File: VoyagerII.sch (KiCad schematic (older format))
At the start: 5 parts, among them U1 ATXMEGA32A4U-AU

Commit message: Voltage tests
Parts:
- added C?: 1u, symbol C_Small
- added D?: D_Schottky_Small, symbol D_Schottky_Small
- added U?: MCP1700T-3002E/TT, TO_SOT_Packages_SMD:SOT-23, symbol MCP1700-3002E_SOT23
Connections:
- net +5V: now also U?.3 (VI)
- net GND: now also C?.2, U?.1 (GND)
- new net: C?.1, D?.2 (A), U?.2 (VO)
- new net +3V3: D?.1 (K)
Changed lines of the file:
@@
+	1    0    0    -1
+$EndComp
+$Comp
+L MCP1700-3002E_SOT23 U?
+U 1 1 5A6246D3
+P 3950 1175
+F 0 "U?" H 3800 1300 50  0000 C CNN
+F 1 "MCP1700T-3002E/TT" H 3575 1400 50  0000 L CNN
+F 2 "TO_SOT_Packages_SMD:SOT-23" H 3950 1400 50  0001 C CNN
+F 3 "" H 3950 1175 50  0001 C CNN
+	1    3950 1175
+	1    0    0    -1
+$EndComp
+$Comp
+L +5V #PWR?
+U 1 1 5A624862
+P 3650 1175
+F 0 "#PWR?" H 3650 1025 50  0001 C CNN
+F 1 "+5V" H 3650 1315 50  0000 C CNN
+F 2 "" H 3650 1175 50  0001 C CNN
+F 3 "" H 3650 1175 50  0001 C CNN
+	1    3650 1175
+	0    -1   -1   0
+$EndComp
+$Comp
+L GND #PWR?
+U 1 1 5A6248B2
+P 3950 1475
+F 0 "#PWR?" H 3950 1225 50  0001 C CNN
+F 1 "GND" H 3950 1325 50  0000 C CNN
+F 2 "" H 3950 1475 50  0001 C CNN
+F 3 "" H 3950 1475 50  0001 C CNN
+	1    3950 1475
+	1    0    0    -1
+$EndComp
+$Comp
+L C_Small C?
+U 1 1 5A6248D2
+P 4325 1275
+F 0 "C?" H 4335 1345 50  0000 L CNN
+F 1 "1u" H 4335 1195 50  0000 L CNN
+F 2 "" H 4325 1275 50  0001 C CNN
+F 3 "" H 4325 1275 50  0001 C CNN
+	1    4325 1275
+	1    0    0    -1
+$EndComp
+Wire Wire Line
+	4250 1175 4525 1175
+$Comp
+L D_Schottky_Small D?
+U 1 1 5A624ACB
+P 4625 1175
+F 0 "D?" H 4575 1255 50  0000 L CNN
+F 1 "D_Schottky_Small" H 4345 1095 50  0000 L CNN
+F 2 "" V 4625 1175 50  0001 C CNN
+F 3 "" V 4625 1175 50  0001 C CNN
+	1    4625 1175
+	-1   0    0    1
+$EndComp
+Connection ~ 4325 1175
+$Comp
+L +3.3V #PWR?
+U 1 1 5A624B50
+P 4900 1175
+F 0 "#PWR?" H 4900 1025 50  0001 C CNN
+F 1 "+3.3V" H 4900 1315 50  0000 C CNN
+F 2 "" H 4900 1175 50  0001 C CNN
+F 3 "" H 4900 1175 50  0001 C CNN
+	1    4900 1175
+	-1   0    0    1
+$EndComp
+Wire Wire Line
+	4900 1175 4725 1175
+$Comp
+L GND #PWR?
+U 1 1 5A624D2D
+P 4325 1375
+F 0 "#PWR?" H 4325 1125 50  0001 C CNN
+F 1 "GND" H 4325 1225 50  0000 C CNN
+F 2 "" H 4325 1375 50  0001 C CNN
+F 3 "" H 4325 1375 50  0001 C CNN
+	1    4325 1375
 	1    0    0    -1
 $EndComp

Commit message: Continue schematic
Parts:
- added R?: 10k, symbol R_Small
- added R? (x2): R_Small, symbol R_Small
- added SW?: SW_PUSH, symbol SW_PUSH
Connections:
- net +3V3: now also R?.1
- net +5V: now also R?.2
- net GND: now also R?.1, SW?.1
- net D-: now reaches U1.26 (PD6/D-/RXD1/MISO)
- net D+: now reaches U1.27 (PD7/D+/TXD1/SCK/CLKOUT/EVOUT)
- net at U1.32 (PE2/OC0C/RXD0): now also R?.1, R?.2
- net at U1.35 (~RESET~/PDI_CLK): now also R?.2, SW?.2
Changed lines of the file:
@@
 LIBS:switches
 LIBS:relays
-LIBS:motors
 LIBS:transistors
 LIBS:conn
@@
 	1    0    0    -1
 $EndComp
+$Comp
+L R_Small R?
+U 1 1 5A62554E
+P 2675 3075
+F 0 "R?" H 2705 3095 50  0000 L CNN
+F 1 "10k" H 2705 3035 50  0000 L CNN
+F 2 "" H 2675 3075 50  0000 C CNN
+F 3 "" H 2675 3075 50  0000 C CNN
+	1    2675 3075
+	1    0    0    -1
+$EndComp
+Wire Wire Line
+	2675 3175 2900 3175
+$Comp
+L +3.3V #PWR?
+U 1 1 5A625634
+P 2675 2975
+F 0 "#PWR?" H 2675 2825 50  0001 C CNN
+F 1 "+3.3V" H 2675 3115 50  0000 C CNN
+F 2 "" H 2675 2975 50  0000 C CNN
+F 3 "" H 2675 2975 50  0000 C CNN
+	1    2675 2975
+	1    0    0    -1
+$EndComp
+$Comp
+L SW_PUSH SW?
+U 1 1 5A62565A
+P 2375 3175
+F 0 "SW?" H 2525 3285 50  0000 C CNN
+F 1 "SW_PUSH" H 2375 3095 50  0000 C CNN
+F 2 "" H 2375 3175 50  0000 C CNN
+F 3 "" H 2375 3175 50  0000 C CNN
+	1    2375 3175
+	1    0    0    -1
+$EndComp
+$Comp
+L GND #PWR?
+U 1 1 5A625723
+P 2075 3175
+F 0 "#PWR?" H 2075 2925 50  0001 C CNN
+F 1 "GND" H 2075 3025 50  0000 C CNN
+F 2 "" H 2075 3175 50  0000 C CNN
+F 3 "" H 2075 3175 50  0000 C CNN
+	1    2075 3175
+	0    1    1    0
+$EndComp
+$Comp
+L R_Small R?
+U 1 1 5A6258EE
+P 2525 4050
+F 0 "R?" H 2555 4070 50  0000 L CNN
+F 1 "R_Small" H 2555 4010 50  0000 L CNN
+F 2 "" H 2525 4050 50  0000 C CNN
+F 3 "" H 2525 4050 50  0000 C CNN
+	1    2525 4050
+	-1   0    0    1
+$EndComp
+$Comp
+L R_Small R?
+U 1 1 5A625956
+P 2525 4400
+F 0 "R?" H 2555 4420 50  0000 L CNN
+F 1 "R_Small" H 2555 4360 50  0000 L CNN
+F 2 "" H 2525 4400 50  0000 C CNN
+F 3 "" H 2525 4400 50  0000 C CNN
+	1    2525 4400
+	-1   0    0    1
+$EndComp
+Wire Wire Line
+	2525 4150 2525 4300
+Wire Wire Line
+	2900 4225 2525 4225
+Connection ~ 2525 4225
+$Comp
+L +5V #PWR?
+U 1 1 5A6259CA
+P 2525 3950
+F 0 "#PWR?" H 2525 3800 50  0001 C CNN
+F 1 "+5V" H 2525 4090 50  0000 C CNN
+F 2 "" H 2525 3950 50  0000 C CNN
+F 3 "" H 2525 3950 50  0000 C CNN
+	1    2525 3950
+	1    0    0    -1
+$EndComp
+$Comp
+L GND #PWR?
+U 1 1 5A6259F6
+P 2525 4500
+F 0 "#PWR?" H 2525 4250 50  0001 C CNN
+F 1 "GND" H 2525 4350 50  0000 C CNN
+F 2 "" H 2525 4500 50  0000 C CNN
+F 3 "" H 2525 4500 50  0000 C CNN
+	1    2525 4500
+	1    0    0    -1
+$EndComp
+Text GLabel 2900 5075 0    60   Input ~ 0
+D-
+Text GLabel 2900 5175 0    60   Input ~ 0
+D+
 $EndSCHEMATC

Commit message: Add libs
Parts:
- added C? (x5): 0.1u, symbol C_Small
- added C?: 4.7u, symbol C_Small
- added P?: TC2030-IDC, symbol TC2030-IDC
- R? (x2): value R_Small -> 100k
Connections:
- net +3V3: now also U1.19 (VCC), U1.31 (VCC), U1.39 (AVCC), U1.9 (VCC), C?.1, C?.1, C?.1, C?.1, C?.1
- net GND: now also U1.18 (GND), U1.30 (GND), U1.38 (GND), U1.8 (GND), C?.1, C?.2, C?.2, C?.2, C?.2, C?.2, C?.2, P?.2 (P2), P?.6 (P6)
- net PDI: now reaches U1.34 (PDI_DATA)
- net PDI: now also P?.1 (P1)
- net PDI_CLK: now reaches R?.2, SW?.2, U1.35 (~RESET~/PDI_CLK)
- net PDI_CLK: now also P?.5 (P5)
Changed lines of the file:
@@
 LIBS:MX_Alps_Hybrids
 LIBS:ws2812b
+LIBS:Tag-Connect
 LIBS:VoyagerII-cache
 EELAYER 25 0
@@
 P 2525 4050
 F 0 "R?" H 2555 4070 50  0000 L CNN
-F 1 "R_Small" H 2555 4010 50  0000 L CNN
+F 1 "100k" H 2555 4010 50  0000 L CNN
 F 2 "" H 2525 4050 50  0000 C CNN
 F 3 "" H 2525 4050 50  0000 C CNN
@@
 P 2525 4400
 F 0 "R?" H 2555 4420 50  0000 L CNN
-F 1 "R_Small" H 2555 4360 50  0000 L CNN
+F 1 "100k" H 2555 4360 50  0000 L CNN
 F 2 "" H 2525 4400 50  0000 C CNN
 F 3 "" H 2525 4400 50  0000 C CNN
@@
 Text GLabel 2900 5175 0    60   Input ~ 0
 D+
+$Comp
+L TC2030-IDC P?
+U 1 1 5A625E7B
+P 1350 2525
+F 0 "P?" H 1300 2325 40  0000 L CNN
+F 1 "TC2030-IDC" H 1350 2725 40  0000 C CNN
+F 2 "" H 1350 2525 60  0000 C CNN
+F 3 "" H 1350 2525 60  0000 C CNN
+	1    1350 2525
+	1    0    0    -1
+$EndComp
+Text GLabel 1100 2425 0    60   Input ~ 0
+PDI
+Text GLabel 1100 2625 0    60   Input ~ 0
+PDI_CLK
+$Comp
+L GND #PWR?
+U 1 1 5A62606A
+P 1600 2625
+F 0 "#PWR?" H 1600 2375 50  0001 C CNN
+F 1 "GND" H 1600 2475 50  0000 C CNN
+F 2 "" H 1600 2625 50  0000 C CNN
+F 3 "" H 1600 2625 50  0000 C CNN
+	1    1600 2625
+	0    -1   -1   0
+$EndComp
+$Comp
+L C_Small C?
+U 1 1 5A626098
+P 1650 2325
+F 0 "C?" H 1660 2395 50  0000 L CNN
+F 1 "0.1u" H 1660 2245 50  0000 L CNN
+F 2 "" H 1650 2325 50  0000 C CNN
+F 3 "" H 1650 2325 50  0000 C CNN
+	1    1650 2325
+	1    0    0    -1
+$EndComp
+Wire Wire Line
+	1600 2425 1850 2425
+$Comp
+L GND #PWR?
+U 1 1 5A626190
+P 1650 2225
+F 0 "#PWR?" H 1650 1975 50  0001 C CNN
+F 1 "GND" H 1650 2075 50  0000 C CNN
+F 2 "" H 1650 2225 50  0000 C CNN
+F 3 "" H 1650 2225 50  0000 C CNN
+	1    1650 2225
+	-1   0    0    1
+$EndComp
+$Comp
+L GND #PWR?
+U 1 1 5A6261C0
+P 1850 2425
+F 0 "#PWR?" H 1850 2175 50  0001 C CNN
+F 1 "GND" H 1850 2275 50  0000 C CNN
+F 2 "" H 1850 2425 50  0000 C CNN
+F 3 "" H 1850 2425 50  0000 C CNN
+	1    1850 2425
+	0    -1   -1   0
+$EndComp
+Connection ~ 1650 2425
+Wire Wire Line
+	2900 3175 2900 3000
+Text GLabel 2900 3000 1    60   Input ~ 0
+PDI_CLK
+Text GLabel 2900 3275 0    60   Input ~ 0
+PDI
+Wire Wire Line
+	3700 2875 3700 2725
+Wire Wire Line
+	3700 2725 4100 2725
+Wire Wire Line
+	3800 2725 3800 2875
+Wire Wire Line
+	3900 2725 3900 2875
+Connection ~ 3800 2725
+Wire Wire Line
+	4100 2725 4100 2875
+Connection ~ 3900 2725
+$Comp
+L +3.3V #PWR?
+U 1 1 5A6265F5
+P 3700 2725
+F 0 "#PWR?" H 3700 2575 50  0001 C CNN
+F 1 "+3.3V" H 3700 2865 50  0000 C CNN
+F 2 "" H 3700 2725 50  0000 C CNN
+F 3 "" H 3700 2725 50  0000 C CNN
+	1    3700 2725
+	1    0    0    -1
+$EndComp
+Wire Wire Line
+	3950 5625 3950 5475
+Wire Wire Line
+	3650 5625 3950 5625
+Wire Wire Line
+	3850 5625 3850 5475
+Wire Wire Line
+	3750 5625 3750 5475
+Connection ~ 3850 5625
+Wire Wire Line
+	3650 5625 3650 5475
+Connection ~ 3750 5625
+$Comp
+L GND #PWR?
+U 1 1 5A626934
+P 3950 5625
+F 0 "#PWR?" H 3950 5375 50  0001 C CNN
+F 1 "GND" H 3950 5475 50  0000 C CNN
+F 2 "" H 3950 5625 50  0000 C CNN
+F 3 "" H 3950 5625 50  0000 C CNN
+	1    3950 5625
+	1    0    0    -1
+$EndComp
+$Comp
+L C_Small C?
+U 1 1 5A626BEB
+P 4225 2175
+F 0 "C?" H 4235 2245 50  0000 L CNN
+F 1 "0.1u" H 4235 2095 50  0000 L CNN
+F 2 "" H 4225 2175 50  0000 C CNN
+F 3 "" H 4225 2175 50  0000 C CNN
+	1    4225 2175
+	1    0    0    -1
+$EndComp
+$Comp
+L C_Small C?
+U 1 1 5A626C99
+P 4625 2175
+F 0 "C?" H 4635 2245 50  0000 L CNN
+F 1 "0.1u" H 4635 2095 50  0000 L CNN
+F 2 "" H 4625 2175 50  0000 C CNN
+F 3 "" H 4625 2175 50  0000 C CNN
+	1    4625 2175
+	1    0    0    -1
+$EndComp
+$Comp
+L C_Small C?
+U 1 1 5A626CEB
+P 4825 2175
+F 0 "C?" H 4835 2245 50  0000 L CNN
+F 1 "0.1u" H 4835 2095 50  0000 L CNN
+F 2 "" H 4825 2175 50  0000 C CNN
+F 3 "" H 4825 2175 50  0000 C CNN
+	1    4825 2175
+	1    0    0    -1
+$EndComp
+$Comp
+L C_Small C?
+U 1 1 5A626D3A
+P 4425 2175
+F 0 "C?" H 4435 2245 50  0000 L CNN
+F 1 "0.1u" H 4435 2095 50  0000 L CNN
+F 2 "" H 4425 2175 50  0000 C CNN
+F 3 "" H 4425 2175 50  0000 C CNN
+	1    4425 2175
+	1    0    0    -1
+$EndComp
+$Comp
+L C_Small C?
+U 1 1 5A626DD8
+P 5050 2175
+F 0 "C?" H 5060 2245 50  0000 L CNN
+F 1 "4.7u" H 5060 2095 50  0000 L CNN
+F 2 "" H 5050 2175 50  0000 C CNN
+F 3 "" H 5050 2175 50  0000 C CNN
+	1    5050 2175
+	1    0    0    -1
+$EndComp
+Wire Wire Line
+	4225 2275 5050 2275
+Connection ~ 4825 2275
+Connection ~ 4625 2275
+Connection ~ 4425 2275
+Wire Wire Line
+	4225 2075 5050 2075
+Connection ~ 4425 2075
+Connection ~ 4625 2075
+Connection ~ 4825 2075
+$Comp
+L +3.3V #PWR?
+U 1 1 5A627061
+P 4225 2075
+F 0 "#PWR?" H 4225 1925 50  0001 C CNN
+F 1 "+3.3V" H 4225 2215 50  0000 C CNN
+F 2 "" H 4225 2075 50  0000 C CNN
+F 3 "" H 4225 2075 50  0000 C CNN
+	1    4225 2075
+	1    0    0    -1
+$EndComp
+$Comp
+L GND #PWR?
+U 1 1 5A62709B
+P 4225 2275
+F 0 "#PWR?" H 4225 2025 50  0001 C CNN
+F 1 "GND" H 4225 2125 50  0000 C CNN
+F 2 "" H 4225 2275 50  0000 C CNN
+F 3 "" H 4225 2275 50  0000 C CNN
+	1    4225 2275
+	1    0    0    -1
+$EndComp
 $EndSCHEMATC

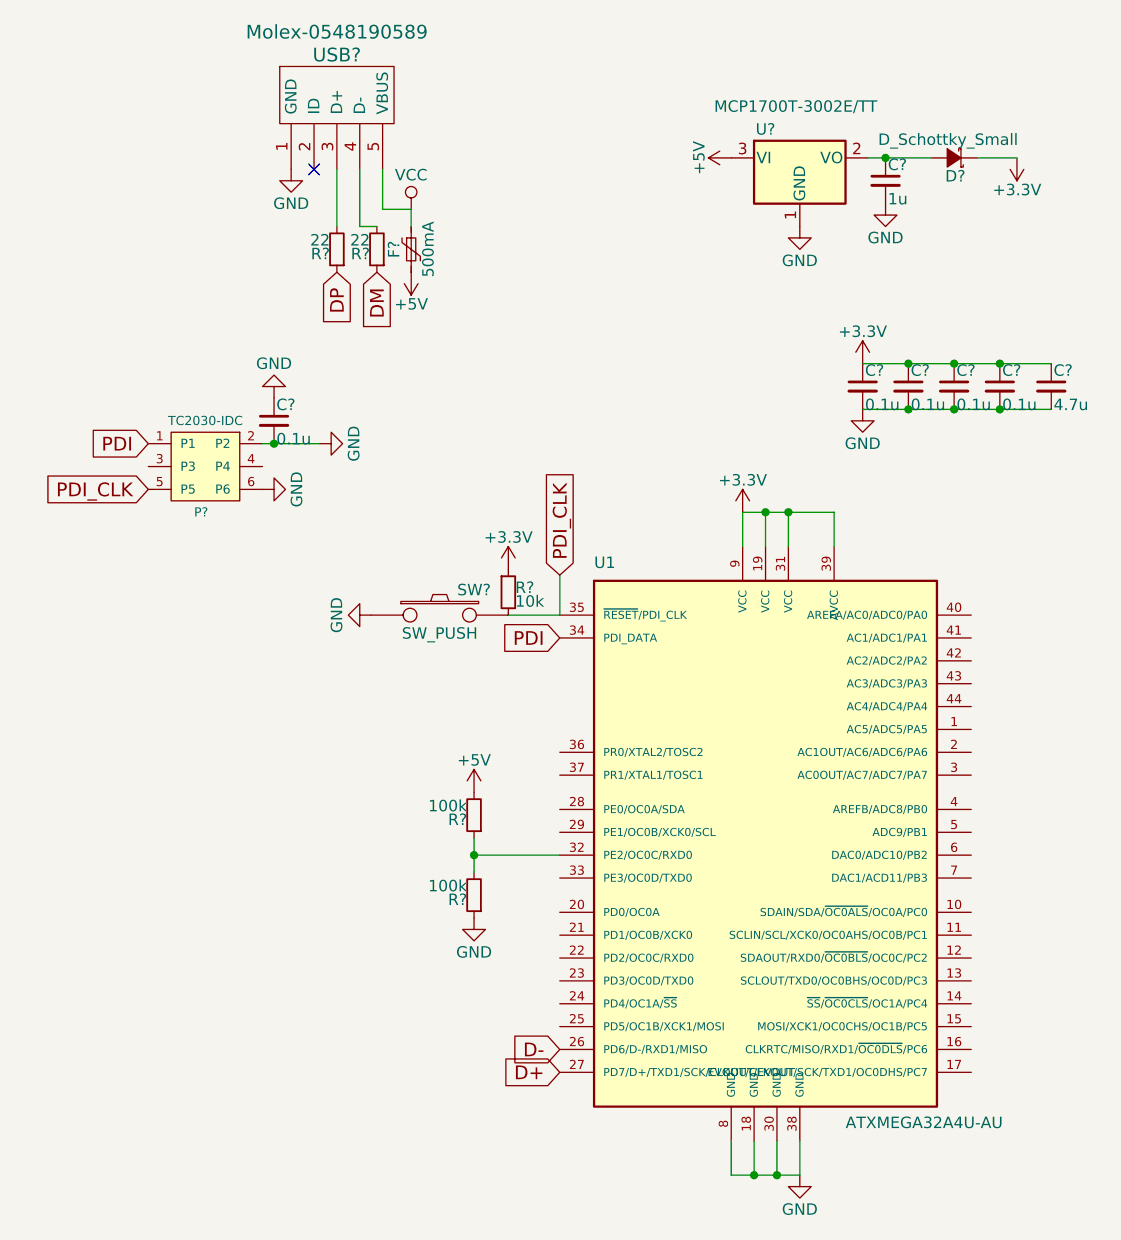
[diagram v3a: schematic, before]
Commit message: Tune up controller to final state
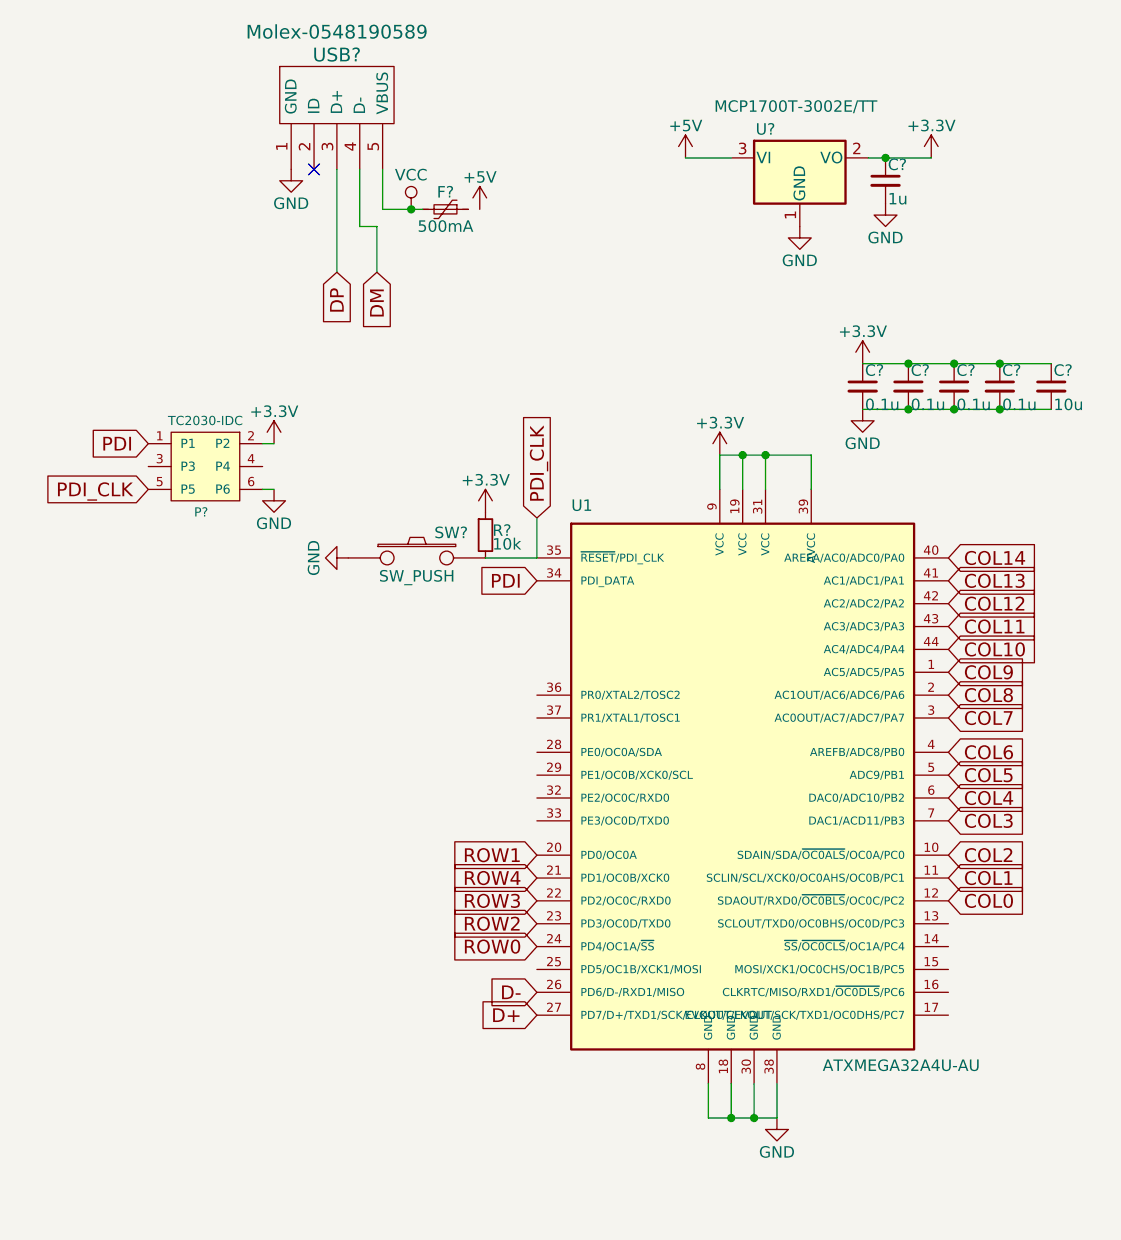
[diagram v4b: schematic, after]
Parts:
- removed C?: 0.1u, symbol C_Small
- removed D?: D_Schottky_Small, symbol D_Schottky_Small
- removed R? (x2): 22, symbol R_Small
- removed R? (x2): 100k, symbol R_Small
- C?: value 4.7u -> 10u
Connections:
- net +3V3: now also C?.1, P?.2 (P2), U?.2 (VO)
- net +5V: no longer F?.2
- net DM: now also USB?.4 (D-)
- net DP: now also USB?.3 (D+)
- net GND: no longer P?.2 (P2)
- net VCC: now also F?.2; no longer F?.1
- net COL9: now reaches U1.1 (AC5/ADC5/PA5)
- net COL2: now reaches U1.10 (SDAIN/SDA/~OC0ALS~/OC0A/PC0)
- net COL1: now reaches U1.11 (SCLIN/SCL/XCK0/OC0AHS/OC0B/PC1)
- net COL0: now reaches U1.12 (SDAOUT/RXD0/~OC0BLS~/OC0C/PC2)
- net COL8: now reaches U1.2 (AC1OUT/AC6/ADC6/PA6)
- net ROW1: now reaches U1.20 (PD0/OC0A)
- net ROW4: now reaches U1.21 (PD1/OC0B/XCK0)
- net ROW3: now reaches U1.22 (PD2/OC0C/RXD0)
- net ROW2: now reaches U1.23 (PD3/OC0D/TXD0)
- net ROW0: now reaches U1.24 (PD4/OC1A/~SS~)
- net COL7: now reaches U1.3 (AC0OUT/AC7/ADC7/PA7)
- net COL6: now reaches U1.4 (AREFB/ADC8/PB0)
- net COL14: now reaches U1.40 (AREFA/AC0/ADC0/PA0)
- net COL13: now reaches U1.41 (AC1/ADC1/PA1)
- net COL12: now reaches U1.42 (AC2/ADC2/PA2)
- net COL11: now reaches U1.43 (AC3/ADC3/PA3)
- net COL10: now reaches U1.44 (AC4/ADC4/PA4)
- net COL5: now reaches U1.5 (ADC9/PB1)
- net COL4: now reaches U1.6 (DAC0/ADC10/PB2)
- net COL3: now reaches U1.7 (DAC1/ACD11/PB3)
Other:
- moved on the sheet: F?, R?, SW?, U1
